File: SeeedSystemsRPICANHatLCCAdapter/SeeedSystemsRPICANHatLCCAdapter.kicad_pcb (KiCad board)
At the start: 2 copper layers, 59.7 x 20.3 mm, 3 parts, among them J1 PC 1737022, J2 Wurth 615008144221, J3 Wurth 615008144221

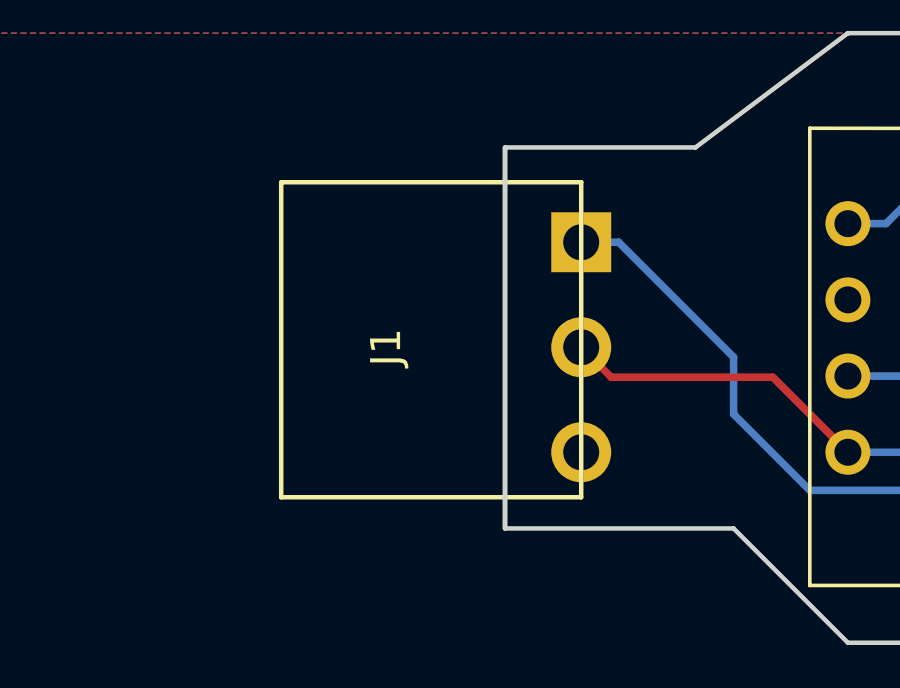
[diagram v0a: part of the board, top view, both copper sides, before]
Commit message: Use generated CAD objects from Mouser
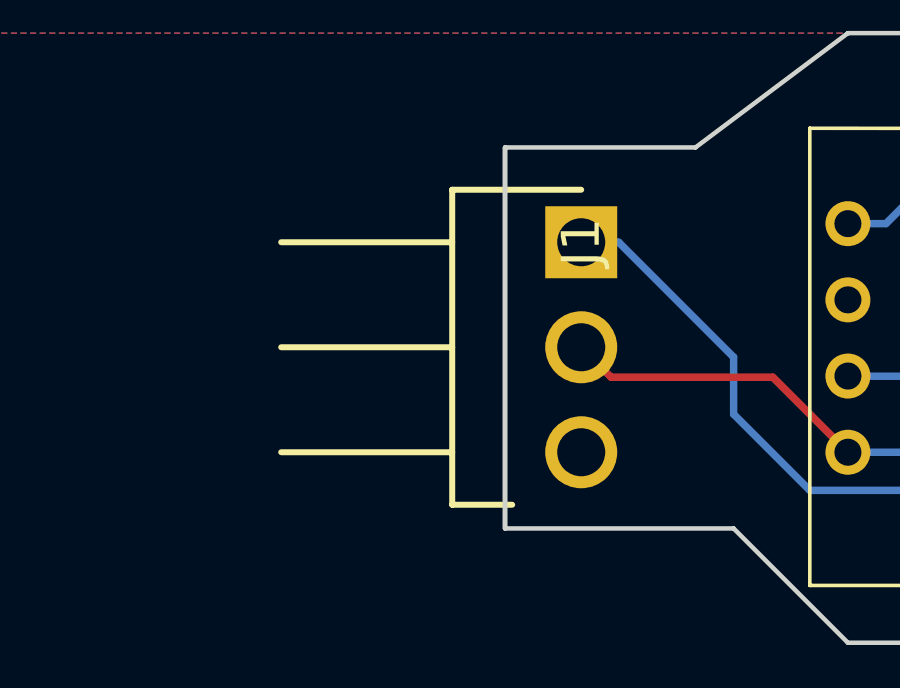
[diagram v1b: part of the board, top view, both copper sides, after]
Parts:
- J1: value PC 1737022 -> 1737022; footprint MyPinHeaders:PinArray_3_RA_3.5MM -> 1737022:HDRRA3W100P0X350_1X3_1050X200X280P
- moved J1 3.50 mm to (101.6, 41.3), turned to 90 degrees
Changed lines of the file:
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@@
     (links 12)
     (no_connects 0)
-    (area 77.47 34.214999 158.825001 57.150001)
+    (area 98.984999 34.214999 158.825001 54.685001)
     (thickness 1.6)
     (drawings 12)
@@
     )
   )
-  (module MyPinHeaders:PinArray_3_RA_3.5MM (layer F.Cu)
-    (at 101.6 44.76 270)
-    (fp_text reference J1 (at 0 6.5 270) (layer F.SilkS)
-      (effects (font (size 1 1) (thickness 0.15)))
-    )
-    (fp_text value "PC 1737022 " (at -0.31 -3.81 270) (layer F.Fab)
-      (effects (font (size 1 1) (thickness 0.15)))
-    )
-    (fp_line (start 5 0) (end -5.5 0) (layer F.SilkS) (width 0.15))
-    (fp_line (start 5 10) (end 5 0) (layer F.SilkS) (width 0.15))
-    (fp_line (start -5.5 10) (end 5 10) (layer F.SilkS) (width 0.15))
-    (fp_line (start -5.5 0) (end -5.5 10) (layer F.SilkS) (width 0.15))
-    (pad 2 thru_hole circle (at 0 0 270) (size 2 2) (drill 1.2) (layers *.Cu *.Mask)
+  (module 1737022:HDRRA3W100P0X350_1X3_1050X200X280P (layer F.Cu)
+    (at 101.6 41.26 90)
+    (descr 1737022)
+    (tags Connector)
+    (fp_text reference J1 (at 0 0 90) (layer F.SilkS)
+      (effects (font (size 1.27 1.27) (thickness 0.254)))
+    )
+    (fp_text value 1737022 (at 0 0 90) (layer F.SilkS) hide
+      (effects (font (size 1.27 1.27) (thickness 0.254)))
+    )
+    (fp_text user %R (at 0 0 90) (layer F.Fab)
+      (effects (font (size 1.27 1.27) (thickness 0.254)))
+    )
+    (fp_line (start 2 1.7) (end -9 1.7) (layer F.CrtYd) (width 0.05))
+    (fp_line (start -9 1.7) (end -9 -10.25) (layer F.CrtYd) (width 0.05))
+    (fp_line (start -9 -10.25) (end 2 -10.25) (layer F.CrtYd) (width 0.05))
+    (fp_line (start 2 -10.25) (end 2 1.7) (layer F.CrtYd) (width 0.05))
+    (fp_line (start 1.75 -2.3) (end -8.75 -2.3) (layer F.Fab) (width 0.1))
+    (fp_line (start -8.75 -2.3) (end -8.75 -4.3) (layer F.Fab) (width 0.1))
+    (fp_line (start -8.75 -4.3) (end 1.75 -4.3) (layer F.Fab) (width 0.1))
+    (fp_line (start 1.75 -4.3) (end 1.75 -2.3) (layer F.Fab) (width 0.1))
+    (fp_line (start 1.75 0) (end 1.75 -4.3) (layer F.SilkS) (width 0.2))
+    (fp_line (start 1.75 -4.3) (end -8.75 -4.3) (layer F.SilkS) (width 0.2))
+    (fp_line (start -8.75 -4.3) (end -8.75 -2.3) (layer F.SilkS) (width 0.2))
+    (fp_line (start 0 -4.3) (end 0 -10) (layer F.SilkS) (width 0.2))
+    (fp_line (start -3.5 -4.3) (end -3.5 -10) (layer F.SilkS) (width 0.2))
+    (fp_line (start -7 -4.3) (end -7 -10) (layer F.SilkS) (width 0.2))
+    (pad 1 thru_hole rect (at 0 0 90) (size 2.4 2.4) (drill 1.6) (layers *.Cu *.Mask)
+      (net 1 /CAN_H))
+    (pad 2 thru_hole circle (at -3.5 0 90) (size 2.4 2.4) (drill 1.6) (layers *.Cu *.Mask)
       (net 2 /CAN_L))
-    (pad 1 thru_hole rect (at -3.5 0 270) (size 2 2) (drill 1.2) (layers *.Cu *.Mask)
-      (net 1 /CAN_H))
-    (pad 3 thru_hole circle (at 3.5 0 270) (size 2 2) (drill 1.2) (layers *.Cu *.Mask)
-      (net 3 GND))
+    (pad 3 thru_hole circle (at -7 0 90) (size 2.4 2.4) (drill 1.6) (layers *.Cu *.Mask)
+      (net 3 GND))
+    (model 1737022.stp
+      (at (xyz 0 0 0))
+      (scale (xyz 1 1 1))
+      (rotate (xyz 0 0 0))
+    )
   )
   (dimension 5.08 (width 0.3) (layer Dwgs.User)
